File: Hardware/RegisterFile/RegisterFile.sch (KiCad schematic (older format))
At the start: 9 parts

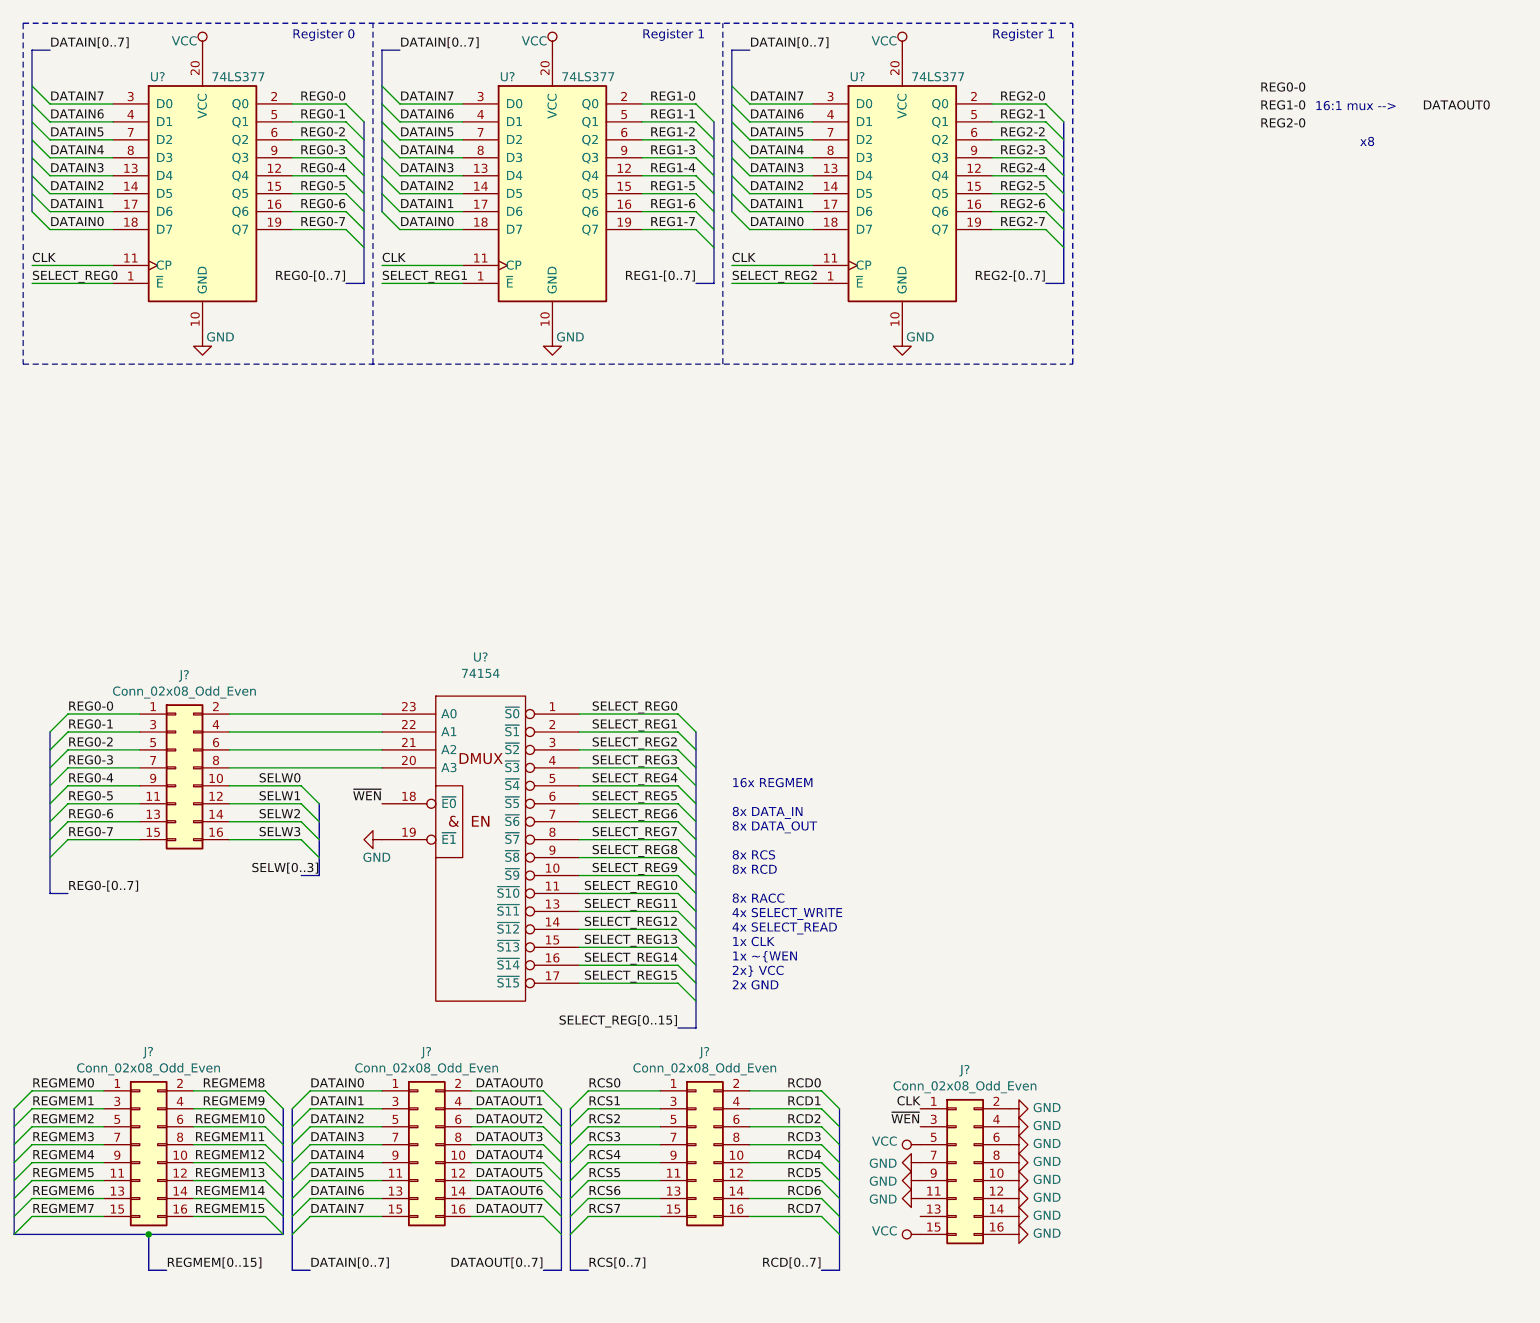
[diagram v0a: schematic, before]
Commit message: Created export for Program Counter PCB V1
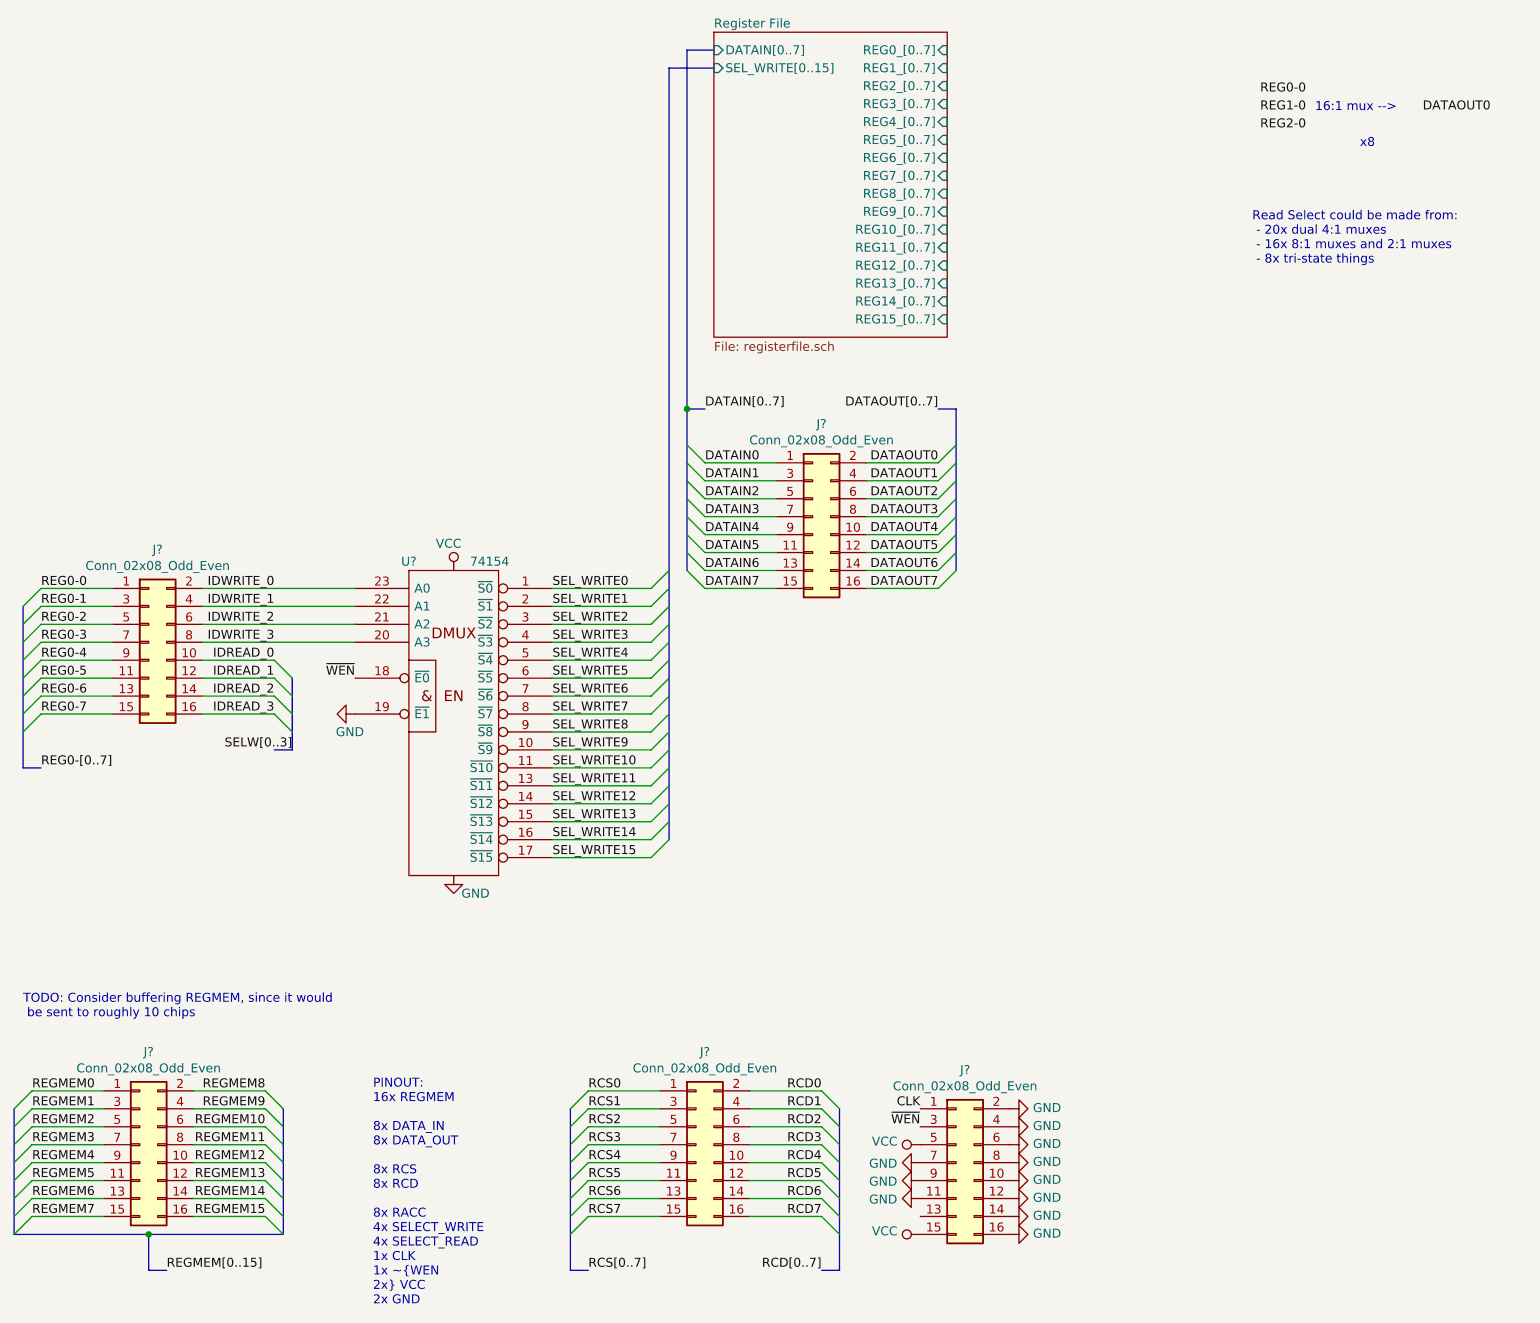
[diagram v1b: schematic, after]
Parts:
- removed U? (x3): 74LS377, symbol 74xx:74LS377
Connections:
- net IDWRITE_3: now reaches J?.8 (Pin_8), U?.20 (A3)
- net IDWRITE_2: now reaches J?.6 (Pin_6), U?.21 (A2)
- net IDWRITE_1: now reaches J?.4 (Pin_4), U?.22 (A1)
- net IDWRITE_0: now reaches J?.2 (Pin_2), U?.23 (A0)
- net SELECT_REG0 renamed SEL_WRITE0
- net SELECT_REG1 renamed SEL_WRITE1
- net SELECT_REG10 renamed SEL_WRITE10
- net SELECT_REG11 renamed SEL_WRITE11
- net SELECT_REG12 renamed SEL_WRITE12
- net SELECT_REG13 renamed SEL_WRITE13
- net SELECT_REG14 renamed SEL_WRITE14
- net SELECT_REG15 renamed SEL_WRITE15
- net SELECT_REG2 renamed SEL_WRITE2
- net SELECT_REG3 renamed SEL_WRITE3
- net SELECT_REG4 renamed SEL_WRITE4
- net SELECT_REG5 renamed SEL_WRITE5
- net SELECT_REG6 renamed SEL_WRITE6
- net SELECT_REG7 renamed SEL_WRITE7
- net SELECT_REG8 renamed SEL_WRITE8
- net SELECT_REG9 renamed SEL_WRITE9
- net SELW0 renamed IDREAD_0
- net SELW1 renamed IDREAD_1
- net SELW2 renamed IDREAD_2
- net SELW3 renamed IDREAD_3
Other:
- note added: "PINOUT:\n16x REGMEM\n\n8x DATA_IN\n8x DATA_OUT\n\n8x RCS\n8x RCD\n\n8x RACC\n4x SELECT_WRITE\n4x SELECT_READ\n1x CLK\n1x ~WEN\n2x VCC\n2x GND"
- note added: "Read Select could be made from:\n - 20x dual 4:1 muxes\n - 16x 8:1 muxes and 2:1 muxes\n - 8x tri-state things"
- note added: "TODO: Consider buffering REGMEM, since it would\n be sent to roughly 10 chips"
- note removed: "16x REGMEM\n\n8x DATA_IN\n8x DATA_OUT\n\n8x RCS\n8x RCD\n\n8x RACC\n4x SELECT_WRITE\n4x SELECT_READ\n1x CLK\n1x ~WEN\n2x VCC\n2x GND"
- note removed: "Register 0"
- note removed: "Register 1"
- moved on the sheet: J?, U?
